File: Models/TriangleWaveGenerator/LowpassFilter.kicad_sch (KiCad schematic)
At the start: 0 parts

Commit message: Filled in breadboard schematic, now need purchase links
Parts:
- added C5: 47 nF, symbol Device:C
- added D1: D, symbol Device:D
- added R1: 100k, symbol Device:R_US
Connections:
- new net: D1.1 (K), R1.1
- new net GND: C5.2
- new net Input: D1.2 (A)
- new net Output: C5.1, R1.2

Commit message: Did the BOM
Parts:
- C5, D1, R1: footprint (none) -> TwoTerminal:THT_10.16mm; now left out of the parts list
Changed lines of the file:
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@@
 		(unit 1)
 		(exclude_from_sim no)
-		(in_bom yes)
+		(in_bom no)
 		(on_board yes)
 		(dnp no)
@@
 			)
 		)
-		(property "Footprint" ""
+		(property "Footprint" "TwoTerminal:THT_10.16mm"
 			(at 146.304 80.264 90)
 			(effects
@@
 		)
 		(property "Description" "Resistor, US symbol"
+			(at 146.05 81.28 0)
+			(effects
+				(font
+					(size 1.27 1.27)
+				)
+				(hide yes)
+			)
+		)
+		(property "Purchase Link" ""
 			(at 146.05 81.28 0)
 			(effects
@@
 		(unit 1)
 		(exclude_from_sim no)
-		(in_bom yes)
+		(in_bom no)
 		(on_board yes)
 		(dnp no)
@@
 			)
 		)
-		(property "Footprint" ""
+		(property "Footprint" "TwoTerminal:THT_10.16mm"
 			(at 153.3652 91.44 0)
 			(effects
@@
 		)
 		(property "Description" "Unpolarized capacitor"
+			(at 152.4 87.63 0)
+			(effects
+				(font
+					(size 1.27 1.27)
+				)
+				(hide yes)
+			)
+		)
+		(property "Purchase Link" ""
 			(at 152.4 87.63 0)
 			(effects
@@
 		(unit 1)
 		(exclude_from_sim no)
-		(in_bom yes)
+		(in_bom no)
 		(on_board yes)
 		(dnp no)
@@
 			)
 		)
-		(property "Footprint" ""
+		(property "Footprint" "TwoTerminal:THT_10.16mm"
 			(at 133.35 81.28 0)
 			(effects
@@
 			(at 133.35 81.28 0)
 			(effects
+				(font
+					(size 1.27 1.27)
+				)
+				(hide yes)
+			)
+		)
+		(property "Purchase Link" ""
+			(at 133.35 81.28 0)
+			(effects

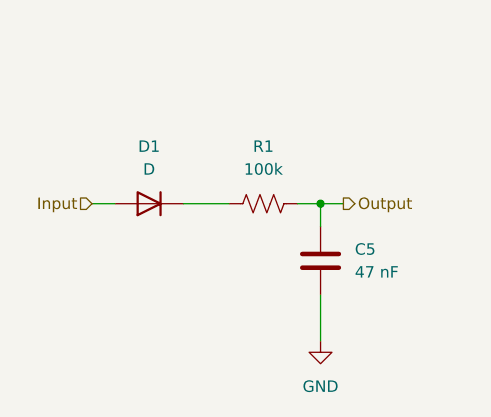
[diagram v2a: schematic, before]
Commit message: Added voltage divider to schematic
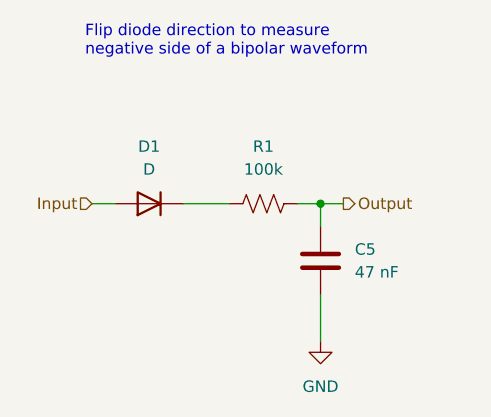
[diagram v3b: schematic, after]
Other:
- note added: "Flip diode direction to measure negative side of a bipolar waveform"
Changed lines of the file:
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@@
 	(generator_version "9.0")
 	(paper "A4")
+	(text "Flip diode direction to measure\nnegative side of a bipolar waveform"
+		(exclude_from_sim no)
+		(at 126.238 61.468 0)
+		(effects
+			(font
+				(size 1.27 1.27)
+			)
+			(justify left top)
+		)
+	)
 	(junction
 		(at 152.4 81.28)
